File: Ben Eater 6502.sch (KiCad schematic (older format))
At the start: 14 parts, among them J1 PS/2 Keyboard, SW1 Reset, SW2 NMI, U1 W65C02SxP, U2 4011, U3 28C256, U4 AS6C62256A, U5 W65C22SxP, U6 74HC74

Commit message: Add integrated eeprom burner
Arduino nano + two 74HC494 shift registers

This is an import from the standalone nano burner.
Still needs to connect to:
* RESB
* RDY
* BE
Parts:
- added A1: Arduino_Nano_v3.x, Module:Arduino_Nano, symbol MCU_Module:Arduino_Nano_v3.x
- added R3, R5: R, symbol Device:R
- added U7, U8: 74HC595, symbol 74xx:74HC595
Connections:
- net +5V: now also U2.14 (VDD), U6.14 (VCC), A1.30 (VIN), R3.2, U7.10 (~SRCLR), U7.16 (VCC), U8.10 (~SRCLR), U8.16 (VCC); no longer DS1.1 (VSS), DS1.16 (LED(-)), J1.2 (Pin_2), RV1.3, SW1.1, SW2.2, U1.21 (VSS), U2.7 (VSS), U3.14 (GND), U3.22 (~OE), U3.27 (~WE), U4.14 (GND), U5.1 (VSS), U6.7 (GND)
- net a0: now also U7.15 (QA)
- net a1: now also U7.1 (QB)
- net a10: now also U8.2 (QC)
- net a11: now also U8.3 (QD)
- net a12: now also U8.4 (QE)
- net a13: now also U8.5 (QF)
- net a14: now also U8.6 (QG)
- net a15: now also U8.7 (QH)
- net a2: now also U7.2 (QC)
- net a3: now also U7.3 (QD)
- net a4: now also U7.4 (QE)
- net a5: now also U7.5 (QF)
- net a6: now also U7.6 (QG)
- net a7: now also U7.7 (QH)
- net a8: now also U8.15 (QA)
- net a9: now also U8.1 (QB)
- net d0: now also A1.11 (D8)
- net d1: now also A1.12 (D9)
- net d2: now also A1.5 (D2)
- net d3: now also A1.6 (D3)
- net d4: now also A1.7 (D4)
- net d5: now also A1.8 (D5)
- net d6: now also A1.9 (D6)
- net d7: now also A1.10 (D7)
- net at R4.2, U1.6 (~NMI): now also SW2.2; no longer SW2.1
- new net: A1.21 (A2), U7.13 (~OE), U8.13 (~OE)
- new net: A1.22 (A3), U7.12 (RCLK)
- new net: A1.23 (A4), U8.12 (RCLK)
- new net: U7.9 (QH'), U8.14 (SER)
- new net GND: A1.29 (GND), A1.4 (GND), DS1.1 (VSS), DS1.16 (LED(-)), J1.2 (Pin_2), R5.1, RV1.3, SW1.1, SW2.1, U1.21 (VSS), U2.7 (VSS), U3.14 (GND), U4.14 (GND), U5.1 (VSS), U6.7 (GND), U7.8 (GND), U8.8 (GND)
- new net MISO_SR_SER: A1.16 (D13), U7.11 (SRCLK), U8.11 (SRCLK)
- new net ROM_OEB: A1.20 (A1), R3.1, U3.27 (~WE)
- new net ROM_WEB: A1.19 (A0), R5.2, U3.22 (~OE)
- new net SCK_SR_SRCLK: A1.14 (D11), U7.14 (SER)
- no-connect marks 13 -> 26
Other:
- note added: "Default Off"
- note added: "Default On\n"
- note added: "PB0"
- note added: "PB1"
- note added: "PB2"
- note added: "PB3"
- note added: "PB4"
- note added: "PB5"
- note added: "PC0"
- note added: "PC1"
- note added: "PC2"
- note added: "PC3"
- note added: "PC4"
- note added: "PC5"
- note added: "PD2"
- note added: "PD3"
- note added: "PD4"
- note added: "PD5"
- note added: "PD6"
- note added: "PD7"
- note added: "SRHI"
- note added: "SRLO"
- moved on the sheet: DS1, J1, R1, R2, R4, RV1, SW1, SW2, U1, U2A, U2B, U2C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

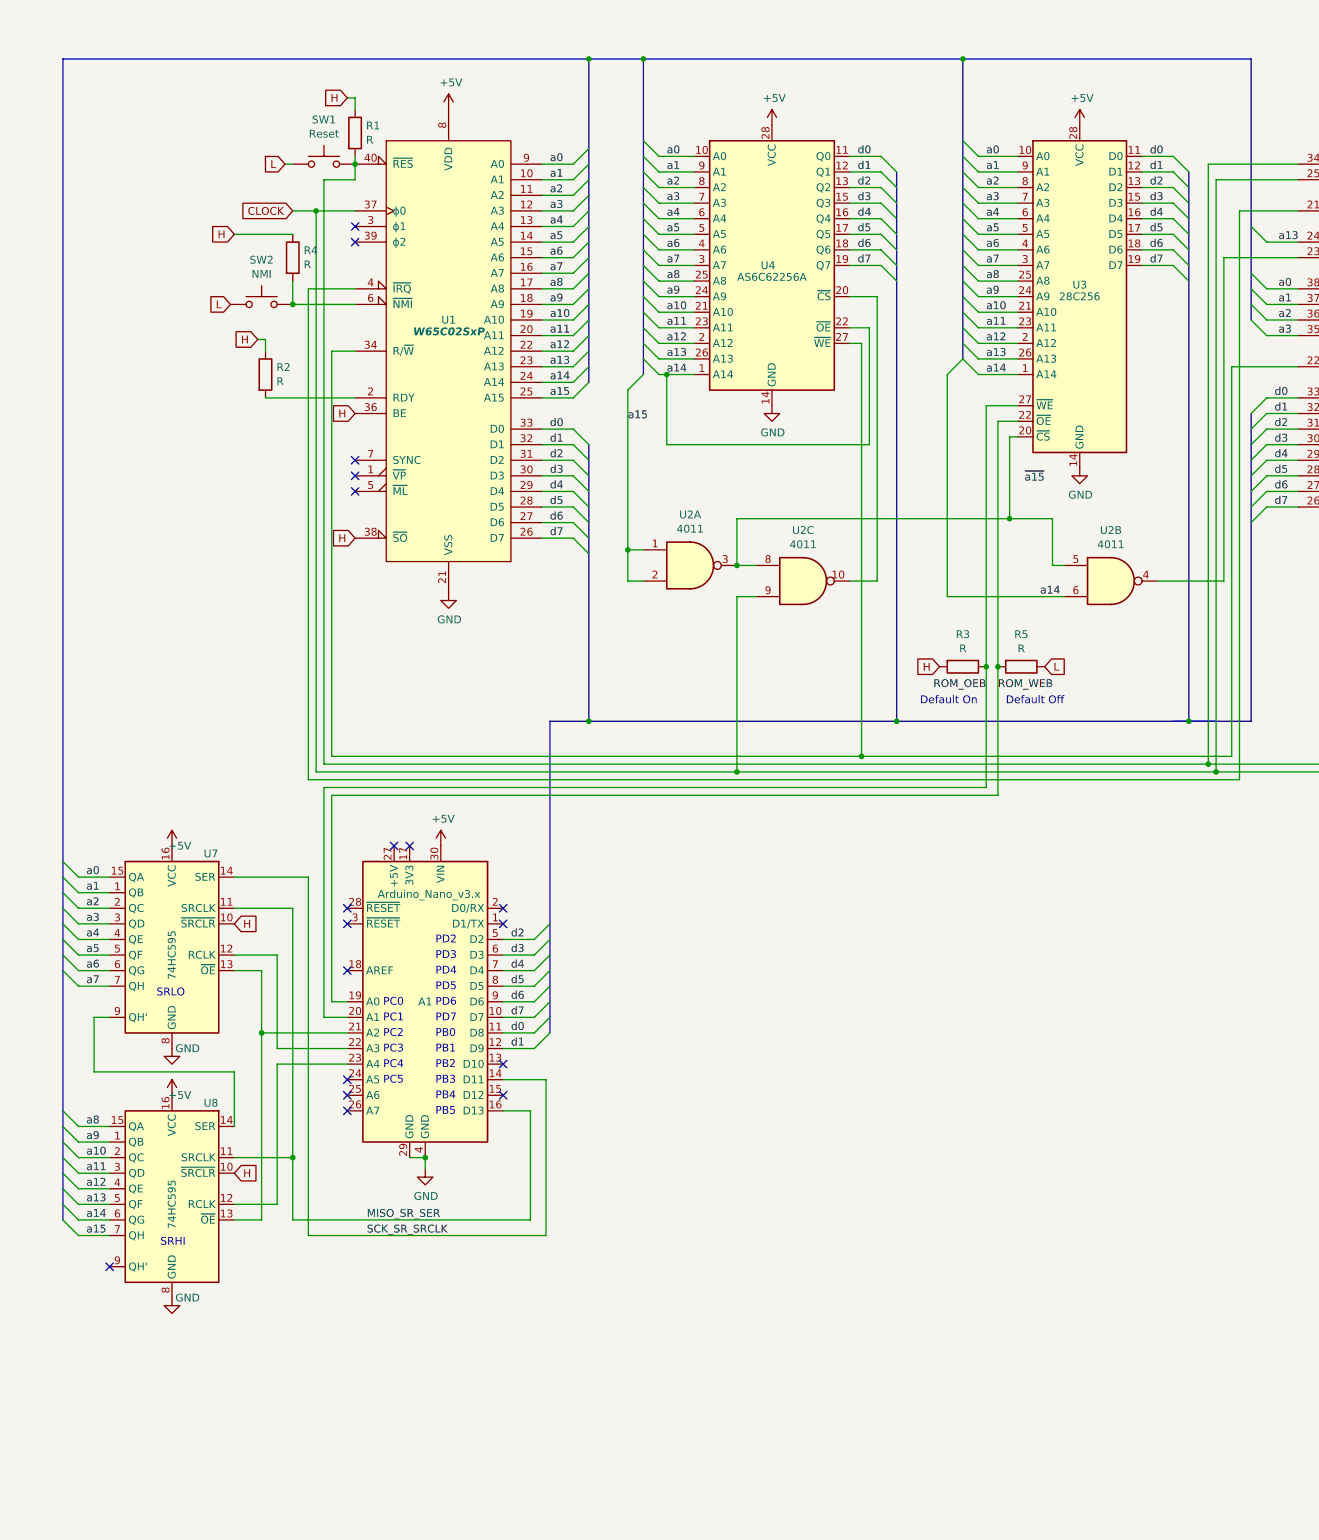
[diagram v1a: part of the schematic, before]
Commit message: Add bus control to integrated eeprom writer
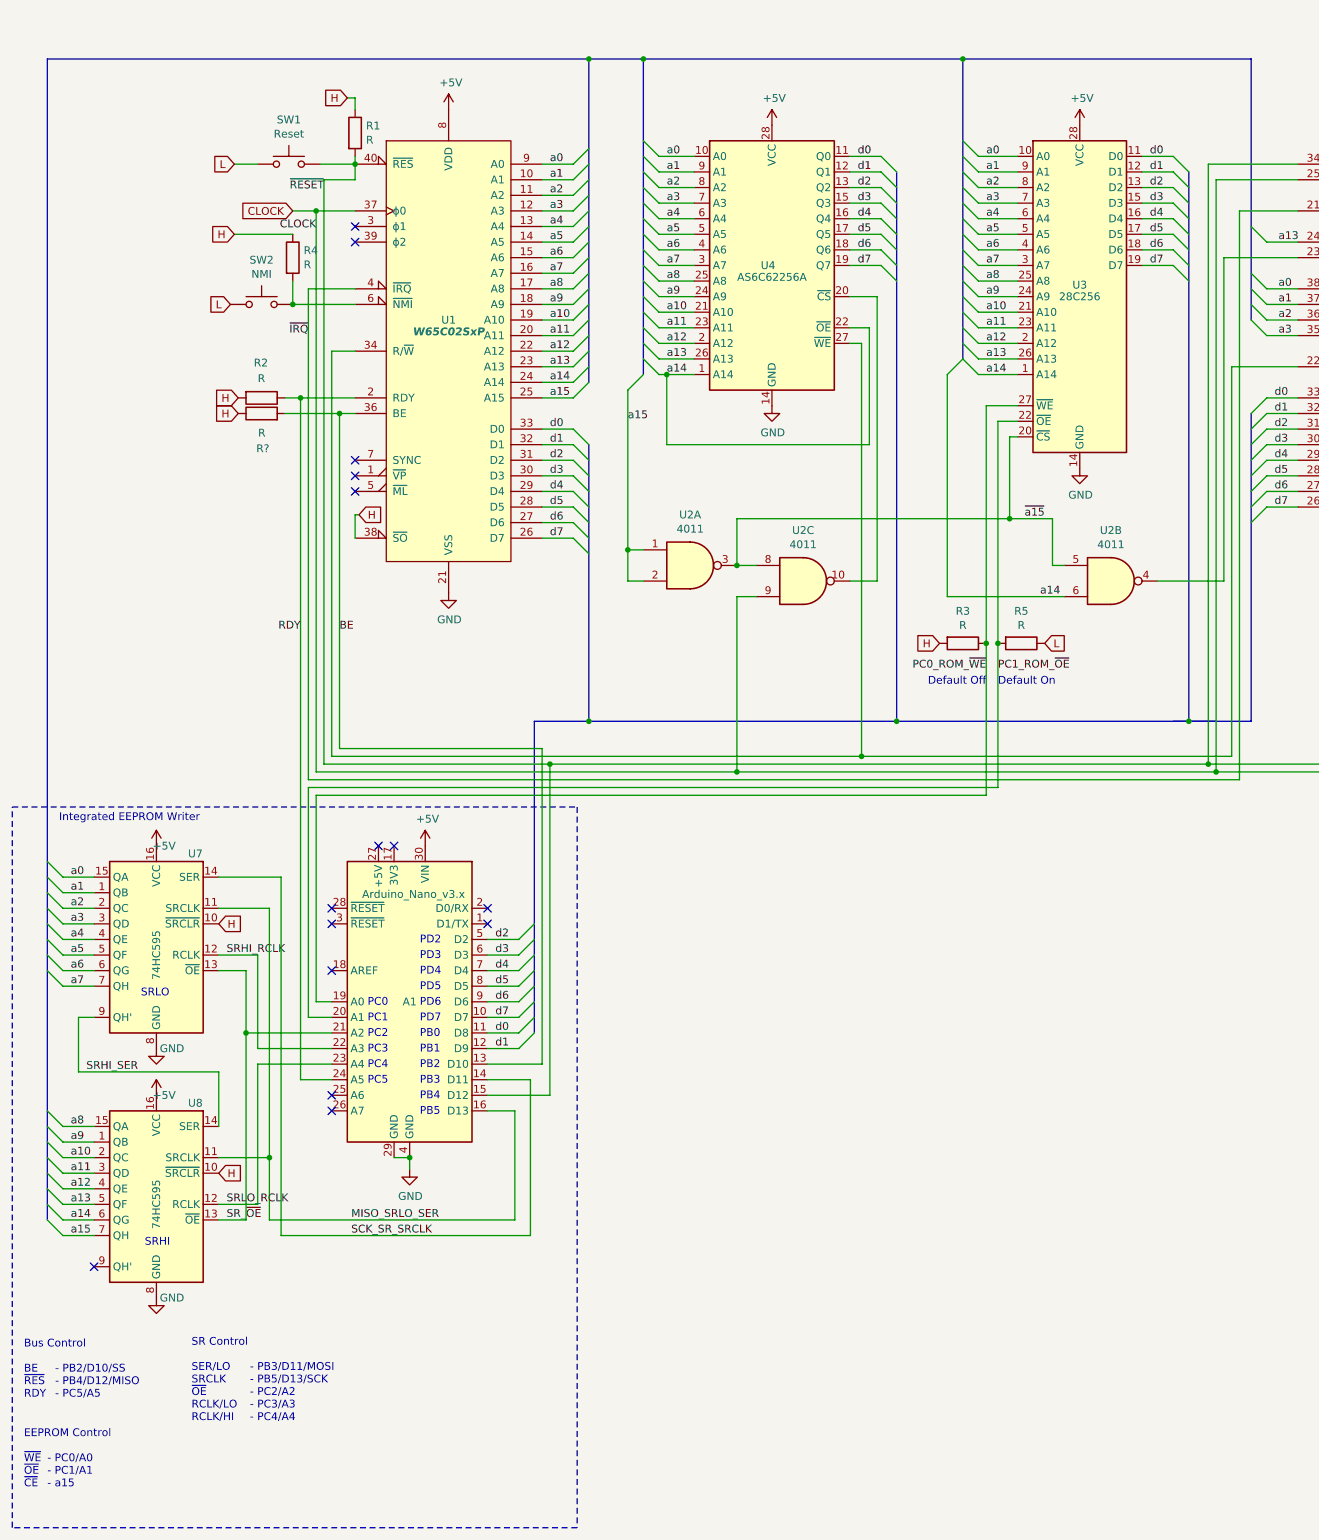
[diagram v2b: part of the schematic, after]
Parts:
- added R?: R, symbol Device:R
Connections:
- net +5V: now also R2.2, R?.1; no longer R2.1, U1.36 (BE)
- net ~a15: now also U2.3, U2.5, U2.8, U3.20 (~CS)
- net RDY: now reaches U1.2 (RDY)
- net RDY: now also A1.24 (A5), R2.1; no longer R2.2
- net ~IRQ~: now reaches U1.4 (~IRQ), U5.21 (~IRQ)
- net ~RESET~: now reaches R1.2, SW1.2, U1.40 (~RES), U5.34 (~RES), U6.4 (~S)
- net ~RESET~: now also A1.15 (D12)
- net BE: now reaches A1.13 (D10)
- net BE: now also U1.36 (BE), R?.2
- net SR_~OE~: now reaches A1.21 (A2), U7.13 (~OE), U8.13 (~OE)
- net SRHI_RCLK: now reaches A1.22 (A3), U7.12 (RCLK)
- net SRLO_RCLK: now reaches A1.23 (A4), U8.12 (RCLK)
- net SRHI_SER: now reaches U7.9 (QH'), U8.14 (SER)
- net MISO_SR_SER renamed MISO_SRLO_SER
- net ROM_OEB renamed PC0_ROM_~WE~
- net PC0_ROM_~WE~: now also A1.19 (A0); no longer A1.20 (A1)
- net ROM_WEB renamed PC1_ROM_~OE~
- net PC1_ROM_~OE~: now also A1.20 (A1); no longer A1.19 (A0)
- no-connect marks 26 -> 23
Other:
- note added: "Bus Control\n\nBE\n~RES~\nRDY"
- note added: "EEPROM Control\n\n~WE~\n~OE~\n~CE~"
- note added: "Integrated EEPROM Writer"
- note added: "SR Control\n\nSER/LO\nSRCLK\n~OE~\nRCLK/LO\nRCLK/HI\n"
- note added: "\n\n- PB2/D10/SS\n- PB4/D12/MISO\n- PC5/A5"
- note added: "\n\n- PB3/D11/MOSI\n- PB5/D13/SCK\n- PC2/A2\n- PC3/A3\n- PC4/A4\n"
- note added: "\n\n- PC0/A0\n- PC1/A1\n- a15"
- moved on the sheet: A1, R2, R3, R5, SW1, U7, U8

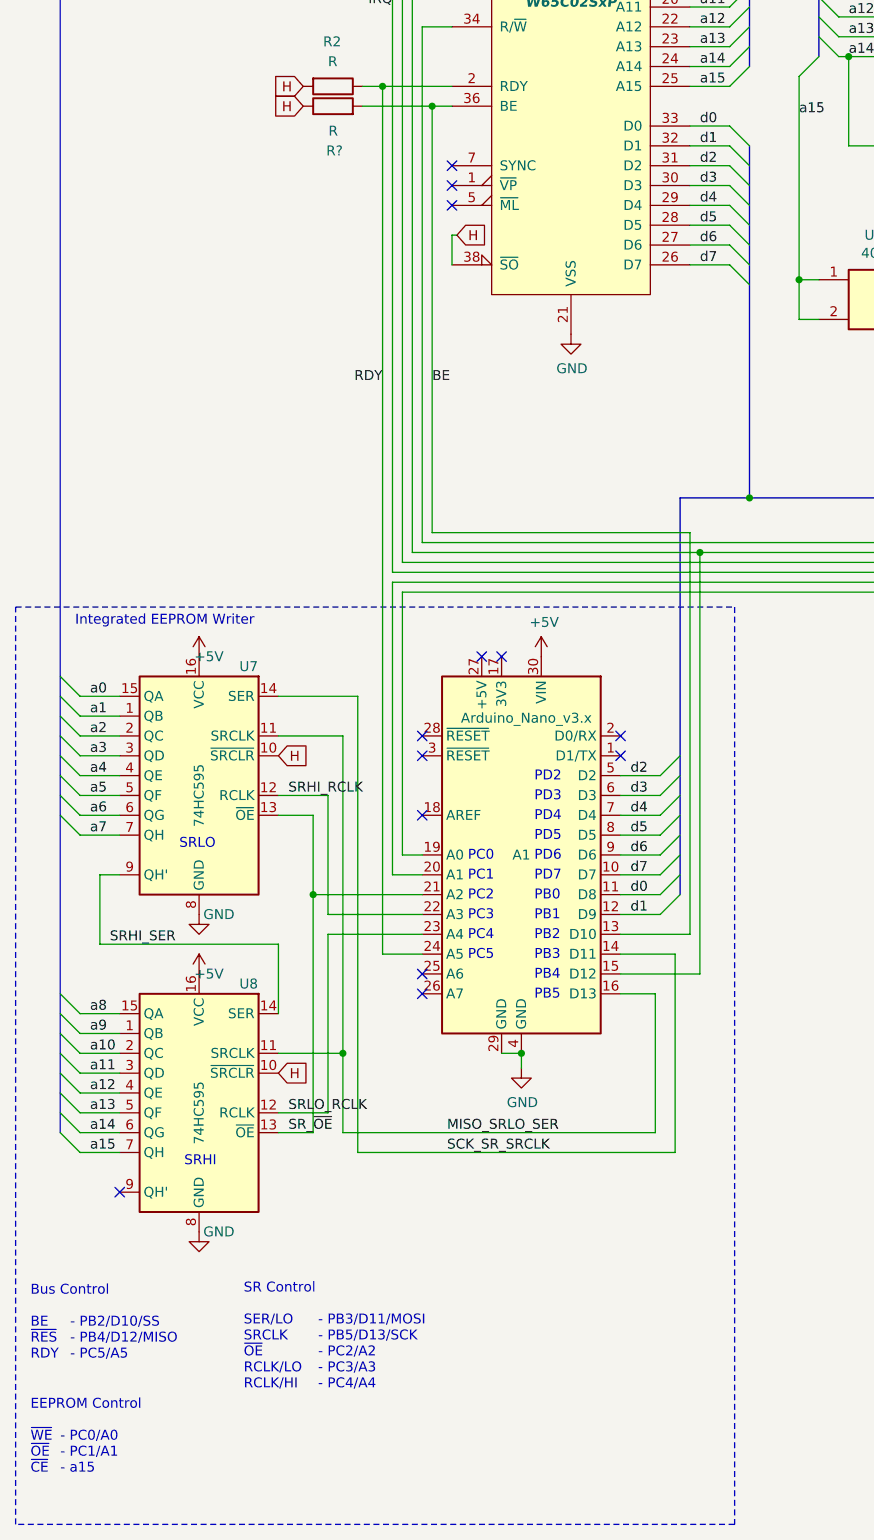
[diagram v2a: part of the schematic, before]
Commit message: Add bus enable disabled indicator
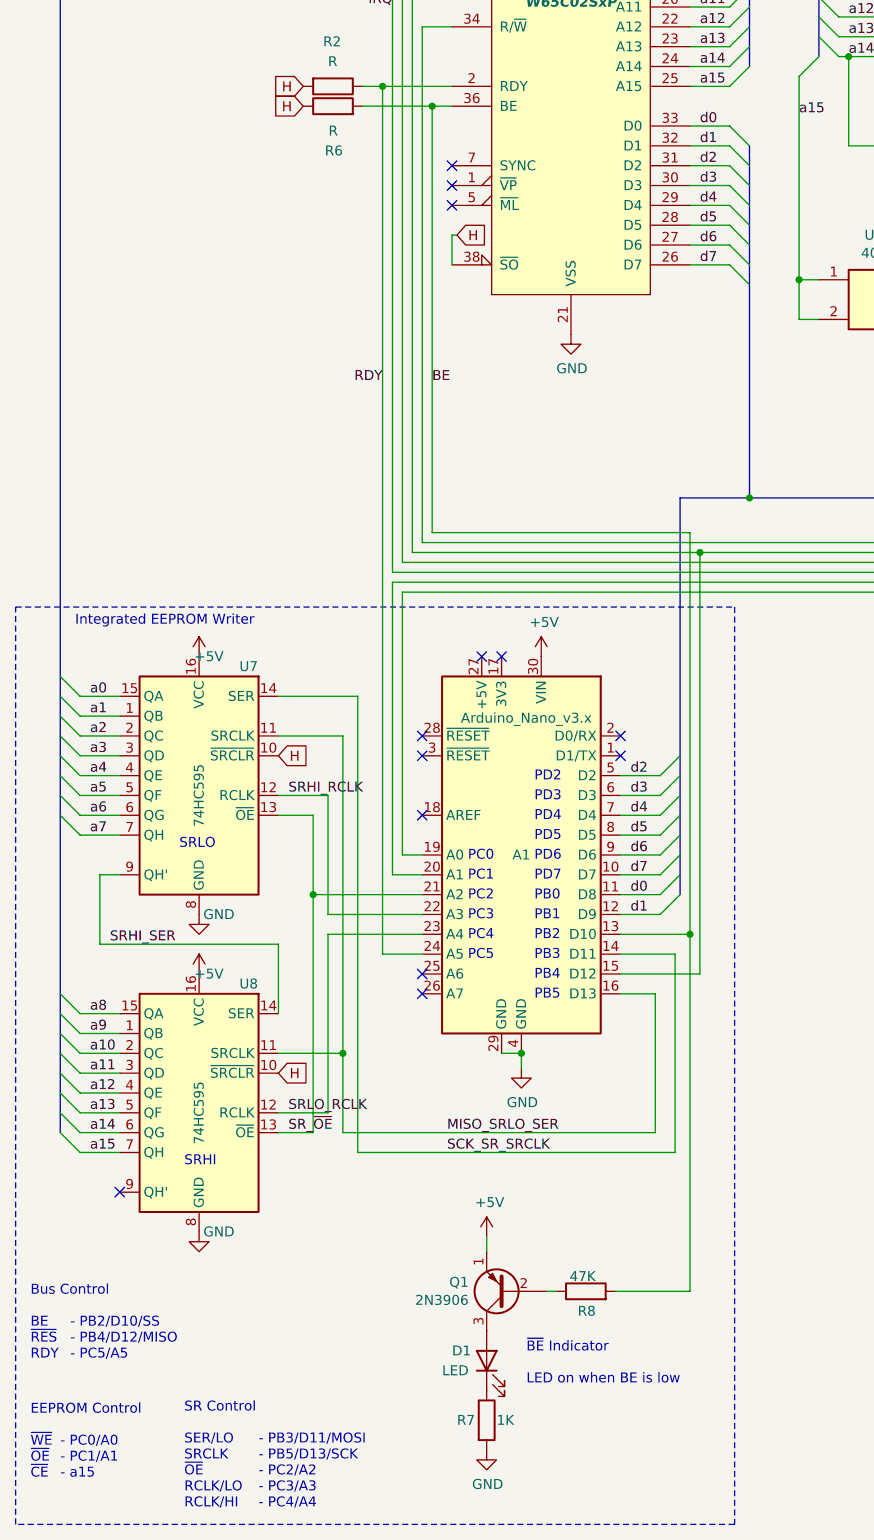
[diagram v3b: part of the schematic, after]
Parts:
- added D1: LED, symbol Device:LED
- added Q1: 2N3906, Package_TO_SOT_THT:TO-92_Inline, symbol Transistor_BJT:2N3906
- added R7: 1K, symbol Device:R
- added R8: 47K, symbol Device:R
- gave numbers to parts that had none: 1
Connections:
- net +5V: now also Q1.1 (E)
- net BE: now also R8.2
- net GND: now also R7.2
- new net: Q1.2 (B), R8.1
- new net: D1.2 (A), Q1.3 (C)
- new net: D1.1 (K), R7.1
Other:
- note added: "~BE~ Indicator\n\nLED on when BE is low"
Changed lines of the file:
@@
 	3350 3325 3700 3325
 $Comp
-L Device:R R?
+L Device:R R6
 U 1 1 61FB3C6F
 P 3100 3425
-F 0 "R?" V 2875 3375 50  0000 L CNN
+F 0 "R6" V 2875 3375 50  0000 L CNN
 F 1 "R" V 2975 3400 50  0000 L CNN
 F 2 "" V 3030 3425 50  0001 C CNN
@@
 Wire Notes Line
 	1500 10575 1500 5950
-Text Notes 1725 10325 0    50   ~ 0
+Text Notes 1725 10350 0    50   ~ 0
 \n\n- PC0/A0\n- PC1/A1\n- a15
-Text Notes 2650 9900 0    50   ~ 0
+Text Notes 2350 10500 0    50   ~ 0
 SR Control\n\nSER/LO\nSRCLK\n~OE~\nRCLK/LO\nRCLK/HI\n
+Text Notes 2725 10500 0    50   ~ 0
+\n\n- PB3/D11/MOSI\n- PB5/D13/SCK\n- PC2/A2\n- PC3/A3\n- PC4/A4\n
+Text Notes 1575 10350 0    50   ~ 0
+EEPROM Control\n\n~WE~\n~OE~\n~CE~
+Text Notes 1575 9750 0    50   ~ 0
+Bus Control\n\nBE\n~RES~\nRDY
+Text Notes 1800 6050 0    50   ~ 0
+Integrated EEPROM Writer
+$Comp
+L Device:R R8
+U 1 1 611B3071
+P 4375 9400
+F 0 "R8" V 4275 9350 50  0000 L CNN
+F 1 "47K" V 4450 9350 50  0000 L CNN
+F 2 "" V 4305 9400 50  0001 C CNN
+F 3 "~" H 4375 9400 50  0001 C CNN
+	1    4375 9400
+	0    -1   -1   0
+$EndComp
+$Comp
+L Device:R R7
+U 1 1 6121FF36
+P 3875 10050
+F 0 "R7" H 3725 10050 50  0000 L CNN
+F 1 "1K" H 3925 10050 50  0000 L CNN
+F 2 "" V 3805 10050 50  0001 C CNN
+F 3 "~" H 3875 10050 50  0001 C CNN
+	1    3875 10050
+	1    0    0    -1
+$EndComp
+Wire Wire Line
+	4900 7600 4900 9400
+Wire Wire Line
+	4900 9400 4525 9400
+Connection ~ 4900 7600
+$Comp
+L power:+5V #PWR019
+U 1 1 61246594
+P 3875 9125
+F 0 "#PWR019" H 3875 8975 50  0001 C CNN
+F 1 "+5V" H 3890 9298 50  0000 C CNN
+F 2 "" H 3875 9125 50  0001 C CNN
+F 3 "" H 3875 9125 50  0001 C CNN
+	1    3875 9125
+	1    0    0    -1
+$EndComp
+$Comp
+L power:GND #PWR020
+U 1 1 6128DE47
+P 3875 10200
+F 0 "#PWR020" H 3875 9950 50  0001 C CNN
+F 1 "GND" H 3880 10027 50  0000 C CNN
+F 2 "" H 3875 10200 50  0001 C CNN
+F 3 "" H 3875 10200 50  0001 C CNN
+	1    3875 10200
+	1    0    0    -1
+$EndComp
+$Comp
+L Device:LED D1
+U 1 1 612218DD
+P 3875 9750
+F 0 "D1" V 3925 9925 50  0000 R CNN
+F 1 "LED" V 3825 9975 50  0000 R CNN
+F 2 "" H 3875 9750 50  0001 C CNN
+F 3 "~" H 3875 9750 50  0001 C CNN
+	1    3875 9750
+	0    -1   -1   0
+$EndComp
+Text Notes 4075 9875 0    50   ~ 0
+~BE~ Indicator\n\nLED on when BE is low
+$Comp
+L Transistor_BJT:2N3906 Q1
+U 1 1 611EE16B
+P 3975 9400
+F 0 "Q1" H 4166 9354 50  0000 L CNN
+F 1 "2N3906" H 4166 9445 50  0000 L CNN
+F 2 "Package_TO_SOT_THT:TO-92_Inline" H 4175 9325 50  0001 L CIN
+F 3 "https://www.onsemi.com/pub/Collateral/2N3906-D.PDF" H 3975 9400 50  0001 L CNN
+	1    3975 9400
+	-1   0    0    1
+$EndComp
+Wire Wire Line
+	3875 9125 3875 9200
+Wire Wire Line
+	4175 9400 4225 9400
 Wire Bus Line
 	9450 1150 9450 2825
@@
 Wire Bus Line
 	5200 1150 5200 3225
-Text Notes 3025 9900 0    50   ~ 0
-\n\n- PB3/D11/MOSI\n- PB5/D13/SCK\n- PC2/A2\n- PC3/A3\n- PC4/A4\n
-Text Notes 1575 10325 0    50   ~ 0
-EEPROM Control\n\n~WE~\n~OE~\n~CE~
-Text Notes 1575 9750 0    50   ~ 0
-Bus Control\n\nBE\n~RES~\nRDY
-Text Notes 1800 6050 0    50   ~ 0
-Integrated EEPROM Writer
 $EndSCHEMATC
